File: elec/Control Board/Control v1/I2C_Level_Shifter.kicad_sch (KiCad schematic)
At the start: 21 parts, among them J201 0.100_2Pin, J202 Conn_01x04, Q201 BSS138, Q202 BSS138

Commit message: Update parts in schematic for BOM generation.
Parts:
- J202: Cost (none) -> 0.0342; Distributor 1 (none) -> JLCPCB; Distributor 1 PN (none) -> C2905415; MPN (none) -> KH-2.54FH-1X4P-H8.5; Manufacturer (none) -> Shenzhen Kinghelm Elec
- R202, R203, R204, R205: MPN RMC 0603 10K F N -> RMC060310KFN
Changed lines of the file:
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@@
       (effects (font (size 1.27 1.27)) hide)
     )
-    (property "Datasheet" "~" (at 129.54 115.57 0)
+    (property "Datasheet" "https://datasheet.lcsc.com/lcsc/1811101310_TyoHM-RMC06031K1-N_C269704.pdf" (at 129.54 115.57 0)
       (effects (font (size 1.27 1.27)) hide)
     )
@@
       (effects (font (size 1.27 1.27)) hide)
     )
-    (property "MPN" "RMC 0603 10K F N" (at 129.54 115.57 0)
+    (property "MPN" "RMC060310KFN" (at 129.54 115.57 0)
       (effects (font (size 1.27 1.27)) hide)
     )
@@
       (effects (font (size 1.27 1.27)) hide)
     )
-    (property "Description" "Do Not Insert" (at 194.31 34.29 0)
+    (property "Description" "DNI" (at 194.31 34.29 0)
       (effects (font (size 1.27 1.27)) hide)
     )
@@
       (effects (font (size 1.27 1.27)) hide)
     )
-    (property "Datasheet" "~" (at 106.68 80.01 0)
+    (property "Datasheet" "https://datasheet.lcsc.com/lcsc/1811101310_TyoHM-RMC06031K1-N_C269704.pdf" (at 106.68 80.01 0)
       (effects (font (size 1.27 1.27)) hide)
     )
@@
       (effects (font (size 1.27 1.27)) hide)
     )
-    (property "MPN" "RMC 0603 10K F N" (at 106.68 80.01 0)
+    (property "MPN" "RMC060310KFN" (at 106.68 80.01 0)
       (effects (font (size 1.27 1.27)) hide)
     )
@@
       (effects (font (size 1.27 1.27)) hide)
     )
-    (property "Datasheet" "~" (at 228.6 95.25 0)
+    (property "Datasheet" "KH-2.54FH-1X4P-H8.5.pdf" (at 228.6 95.25 0)
       (effects (font (size 1.27 1.27)) hide)
     )
     (property "AssemblyType" "HAND" (at 228.6 95.25 0)
+      (effects (font (size 1.27 1.27)) hide)
+    )
+    (property "Cost" "0.0342" (at 228.6 95.25 0)
+      (effects (font (size 1.27 1.27)) hide)
+    )
+    (property "Description" "2.54mm Plugin 3A 4P -40℃~+105℃ Straight 1x4P 8.5mm Top Square Holes Plugin,P=2.54mm Female Headers ROHS" (at 228.6 95.25 0)
+      (effects (font (size 1.27 1.27)) hide)
+    )
+    (property "Distributor 1" "JLCPCB" (at 228.6 95.25 0)
+      (effects (font (size 1.27 1.27)) hide)
+    )
+    (property "Distributor 1 PN" "C2905415" (at 228.6 95.25 0)
+      (effects (font (size 1.27 1.27)) hide)
+    )
+    (property "MPN" "KH-2.54FH-1X4P-H8.5" (at 228.6 95.25 0)
+      (effects (font (size 1.27 1.27)) hide)
+    )
+    (property "Manufacturer" "Shenzhen Kinghelm Elec" (at 228.6 95.25 0)
       (effects (font (size 1.27 1.27)) hide)
     )
@@
       (effects (font (size 1.27 1.27)) hide)
     )
-    (property "Datasheet" "~" (at 129.54 62.23 0)
+    (property "Datasheet" "https://datasheet.lcsc.com/lcsc/1811101310_TyoHM-RMC06031K1-N_C269704.pdf" (at 129.54 62.23 0)
       (effects (font (size 1.27 1.27)) hide)
     )
@@
       (effects (font (size 1.27 1.27)) hide)
     )
-    (property "MPN" "RMC 0603 10K F N" (at 129.54 62.23 0)
+    (property "MPN" "RMC060310KFN" (at 129.54 62.23 0)
       (effects (font (size 1.27 1.27)) hide)
     )
@@
       (effects (font (size 1.27 1.27)) hide)
     )
-    (property "Description" "Do Not Insert" (at 194.31 41.91 0)
+    (property "Description" "DNI" (at 194.31 41.91 0)
       (effects (font (size 1.27 1.27)) hide)
     )
@@
       (effects (font (size 1.27 1.27)) hide)
     )
-    (property "Datasheet" "~" (at 106.68 133.35 0)
+    (property "Datasheet" "https://datasheet.lcsc.com/lcsc/1811101310_TyoHM-RMC06031K1-N_C269704.pdf" (at 106.68 133.35 0)
       (effects (font (size 1.27 1.27)) hide)
     )
@@
       (effects (font (size 1.27 1.27)) hide)
     )
-    (property "MPN" "RMC 0603 10K F N" (at 106.68 133.35 0)
-      (effects (font (size 1.27 1.27)) hide)
-    )
+    (property "MPN" "RMC060310KFN" (at 106.68 133.35 0)
+      (effects (font (size 1.27 1.27)) hide)
+    )

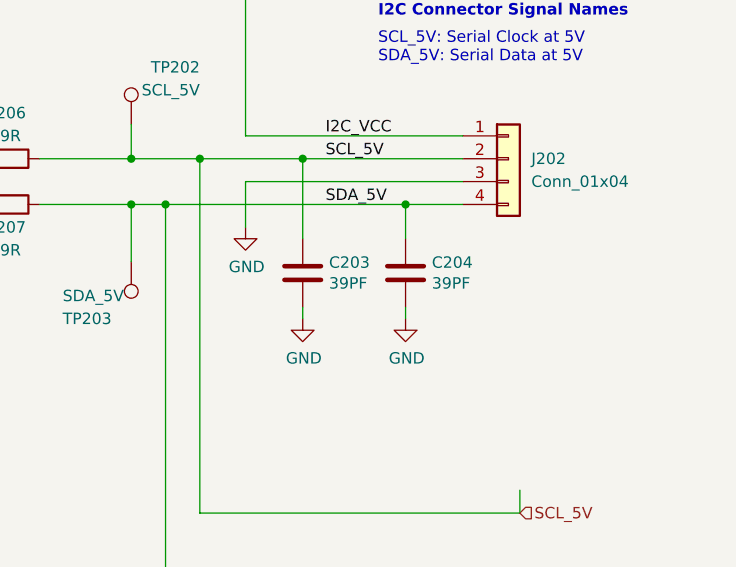
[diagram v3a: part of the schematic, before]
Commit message: Add BOM spread sheet and a JLCPCB BOM.
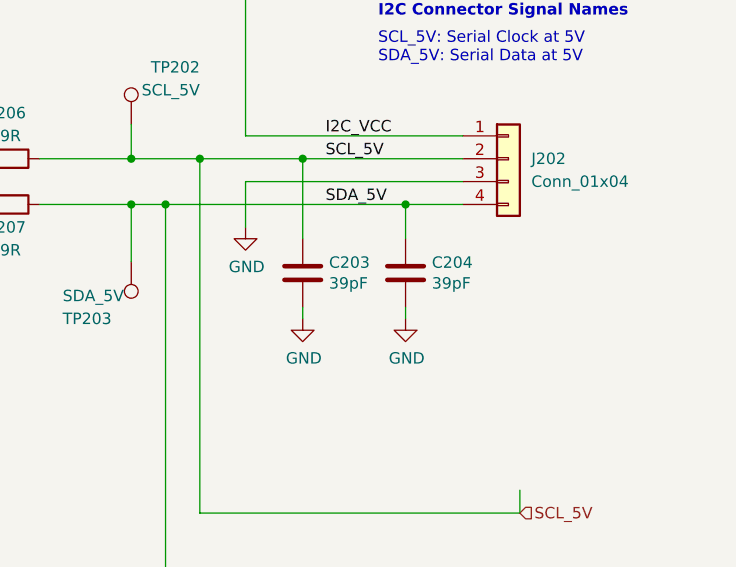
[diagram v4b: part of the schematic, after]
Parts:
- C201, C202: Cost 0.0025 -> 0.0037; Distributor 1 PN (none) -> C91183; MPN (none) -> CC0603JRX7R9BB104
- C203, C204: value 39PF -> 39pF; Cost 0.0025 -> 0.003
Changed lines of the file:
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@@
       (effects (font (size 1.27 1.27)) hide)
     )
-    (property "Datasheet" "https://datasheet.lcsc.com/lcsc/1811082118_YAGEO-CC0603JRNPO9BN390_C107049.pdf" (at 104.14 50.8 0)
+    (property "Datasheet" "CC0603JRX7R9BB104.pdf" (at 104.14 50.8 0)
       (effects (font (size 1.27 1.27)) hide)
     )
@@
       (effects (font (size 1.27 1.27)) hide)
     )
-    (property "Distributor 1 PN" "" (at 104.14 50.8 0)
-      (effects (font (size 1.27 1.27)) hide)
-    )
-    (property "Cost" "0.0025" (at 104.14 50.8 0)
-      (effects (font (size 1.27 1.27)) hide)
-    )
-    (property "MPN" "" (at 104.14 50.8 0)
+    (property "Distributor 1 PN" "C91183" (at 104.14 50.8 0)
+      (effects (font (size 1.27 1.27)) hide)
+    )
+    (property "Cost" "0.0037" (at 104.14 50.8 0)
+      (effects (font (size 1.27 1.27)) hide)
+    )
+    (property "MPN" "CC0603JRX7R9BB104" (at 104.14 50.8 0)
       (effects (font (size 1.27 1.27)) hide)
     )
@@
       (effects (font (size 1.27 1.27)) (justify left))
     )
-    (property "Value" "39PF" (at 220.091 109.093 0)
+    (property "Value" "39pF" (at 220.091 109.093 0)
       (effects (font (size 1.27 1.27)) (justify left))
     )
@@
       (effects (font (size 1.27 1.27)) hide)
     )
-    (property "Cost" "0.0025" (at 217.17 107.95 0)
+    (property "Cost" "0.003" (at 217.17 107.95 0)
       (effects (font (size 1.27 1.27)) hide)
     )
@@
       (effects (font (size 1.27 1.27)) (justify left))
     )
-    (property "Value" "39PF" (at 208.661 109.093 0)
+    (property "Value" "39pF" (at 208.661 109.093 0)
       (effects (font (size 1.27 1.27)) (justify left))
     )
@@
       (effects (font (size 1.27 1.27)) hide)
     )
-    (property "Cost" "0.0025" (at 205.74 107.95 0)
+    (property "Cost" "0.003" (at 205.74 107.95 0)
       (effects (font (size 1.27 1.27)) hide)
     )
@@
       (effects (font (size 1.27 1.27)) hide)
     )
-    (property "Datasheet" "https://datasheet.lcsc.com/lcsc/1811082118_YAGEO-CC0603JRNPO9BN390_C107049.pdf" (at 148.59 31.75 0)
+    (property "Datasheet" "CC0603JRX7R9BB104.pdf" (at 148.59 31.75 0)
       (effects (font (size 1.27 1.27)) hide)
     )
@@
       (effects (font (size 1.27 1.27)) hide)
     )
-    (property "Distributor 1 PN" "" (at 148.59 31.75 0)
-      (effects (font (size 1.27 1.27)) hide)
-    )
-    (property "Cost" "0.0025" (at 148.59 31.75 0)
-      (effects (font (size 1.27 1.27)) hide)
-    )
-    (property "MPN" "" (at 148.59 31.75 0)
-      (effects (font (size 1.27 1.27)) hide)
-    )
+    (property "Distributor 1 PN" "C91183" (at 148.59 31.75 0)
+      (effects (font (size 1.27 1.27)) hide)
+    )
+    (property "Cost" "0.0037" (at 148.59 31.75 0)
+      (effects (font (size 1.27 1.27)) hide)
+    )
+    (property "MPN" "CC0603JRX7R9BB104" (at 148.59 31.75 0)
+      (effects (font (size 1.27 1.27)) hide)
+    )
